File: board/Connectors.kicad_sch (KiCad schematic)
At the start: 14 parts, among them J10 Bus_Hydra_8bit, J11 Bus_Hydra_8bit, J12 Bus_Hydra_8bit, J13 Bus_Hydra_8bit, J14 Bus_Hydra_8bit, J16 SPI_Dev0, J18 SPI_Dev1, J19 SPI_Dev2, J20 SPI_Dev3, J21 SPI_Dev4, J22 SPI_Dev5, J23 SPI_Dev6, J24 SPI_Dev7, J9 Bus_Hydra_8bit

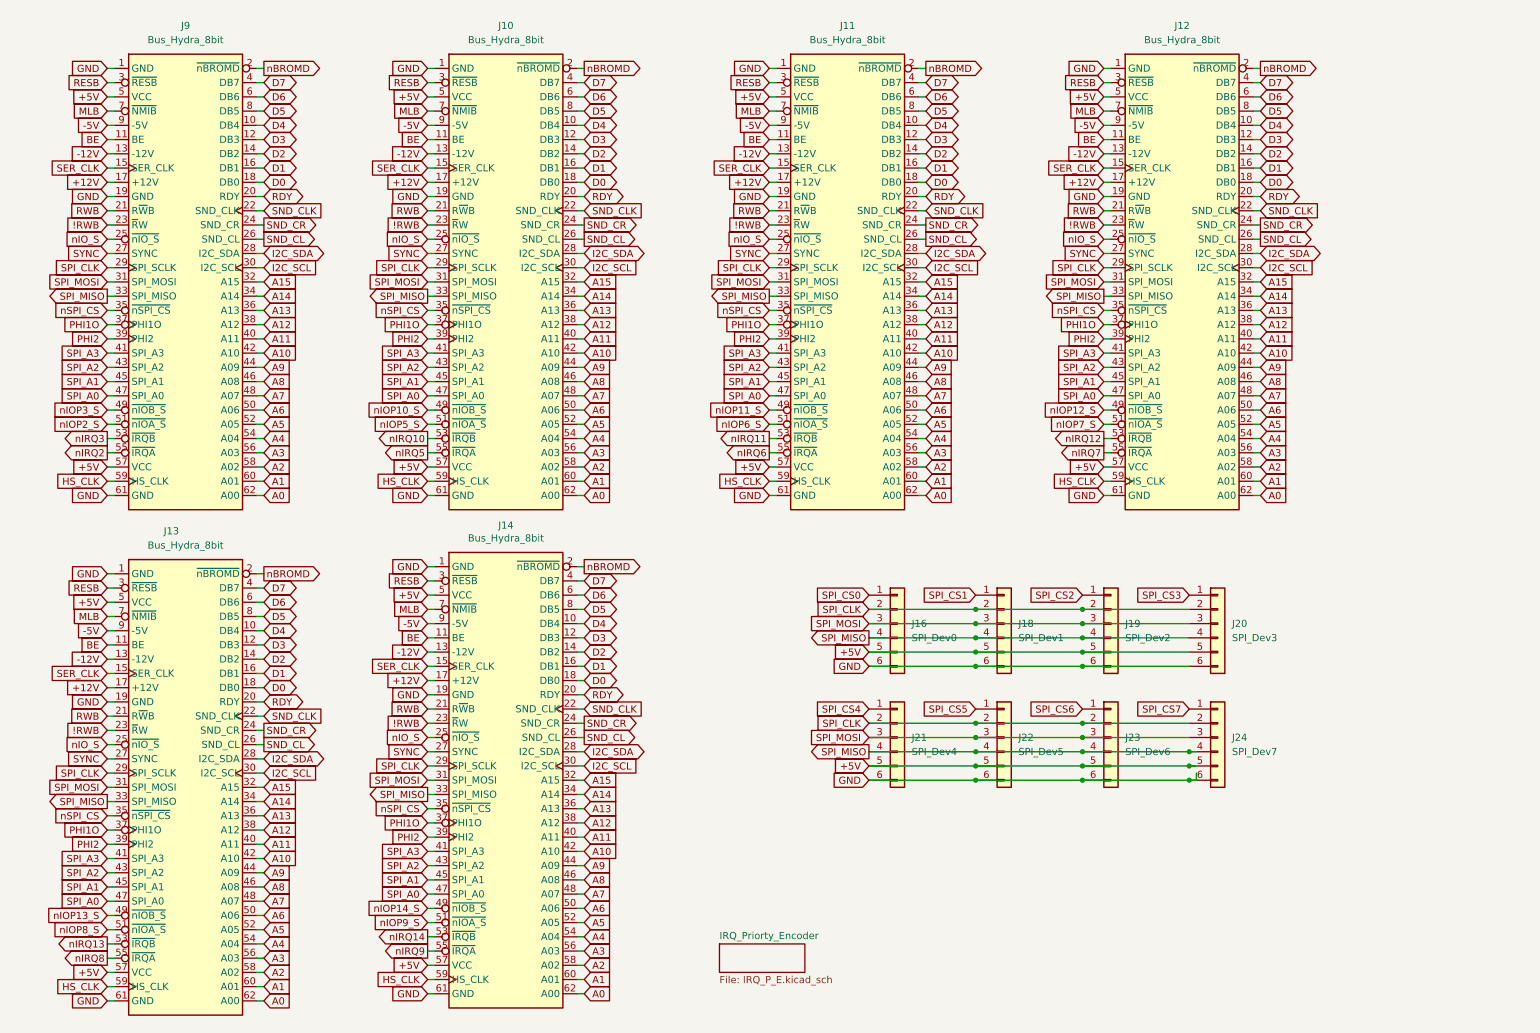
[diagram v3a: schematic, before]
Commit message: Schematic Bus updates, silkscreen updates, position tweaks, and other corrections.
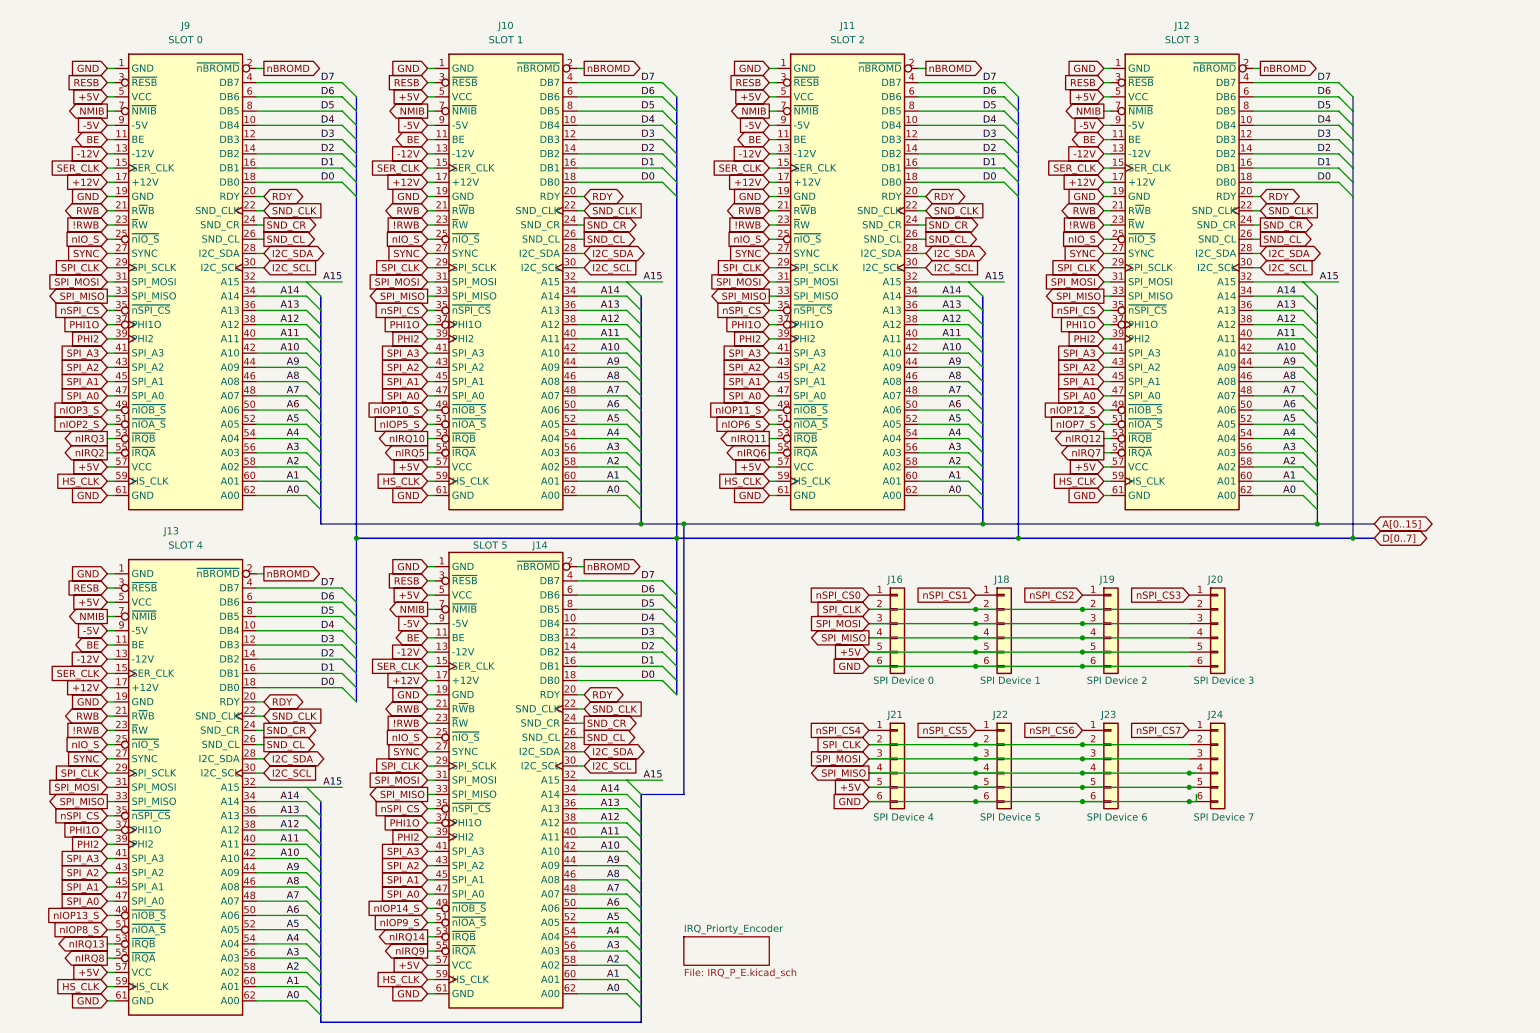
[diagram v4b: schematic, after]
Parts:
- J10: value Bus_Hydra_8bit -> SLOT 1
- J11: value Bus_Hydra_8bit -> SLOT 2
- J12: value Bus_Hydra_8bit -> SLOT 3
- J13: value Bus_Hydra_8bit -> SLOT 4
- J14: value Bus_Hydra_8bit -> SLOT 5
- J16: value SPI_Dev0 -> SPI Device 0
- J18: value SPI_Dev1 -> SPI Device 1
- J19: value SPI_Dev2 -> SPI Device 2
- J20: value SPI_Dev3 -> SPI Device 3
- J21: value SPI_Dev4 -> SPI Device 4
- J22: value SPI_Dev5 -> SPI Device 5
- J23: value SPI_Dev6 -> SPI Device 6
- J24: value SPI_Dev7 -> SPI Device 7
- J9: value Bus_Hydra_8bit -> SLOT 0
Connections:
- net MLB renamed NMIB
- net SPI_CS0 renamed nSPI_CS0
- net SPI_CS1 renamed nSPI_CS1
- net SPI_CS2 renamed nSPI_CS2
- net SPI_CS3 renamed nSPI_CS3
- net SPI_CS4 renamed nSPI_CS4
- net SPI_CS5 renamed nSPI_CS5
- net SPI_CS6 renamed nSPI_CS6
- net SPI_CS7 renamed nSPI_CS7
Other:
- company: (none) -> Data Tuning
- title: (none) -> Card-edge and SPI Device Connectors
- moved on the sheet: J21, J22, J23, J24

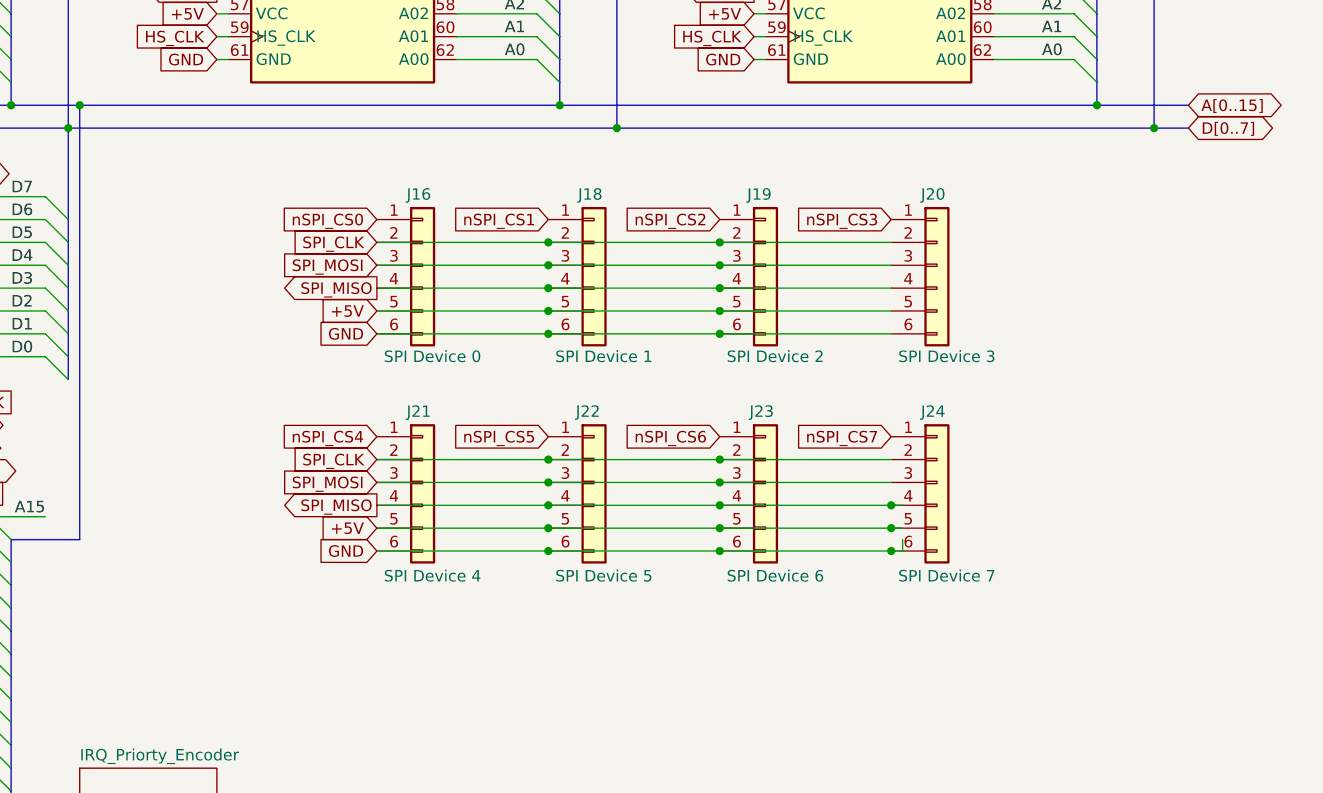
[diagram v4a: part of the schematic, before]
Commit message: Added VIA port A header and voltage protection diode package socket. Updated logic.
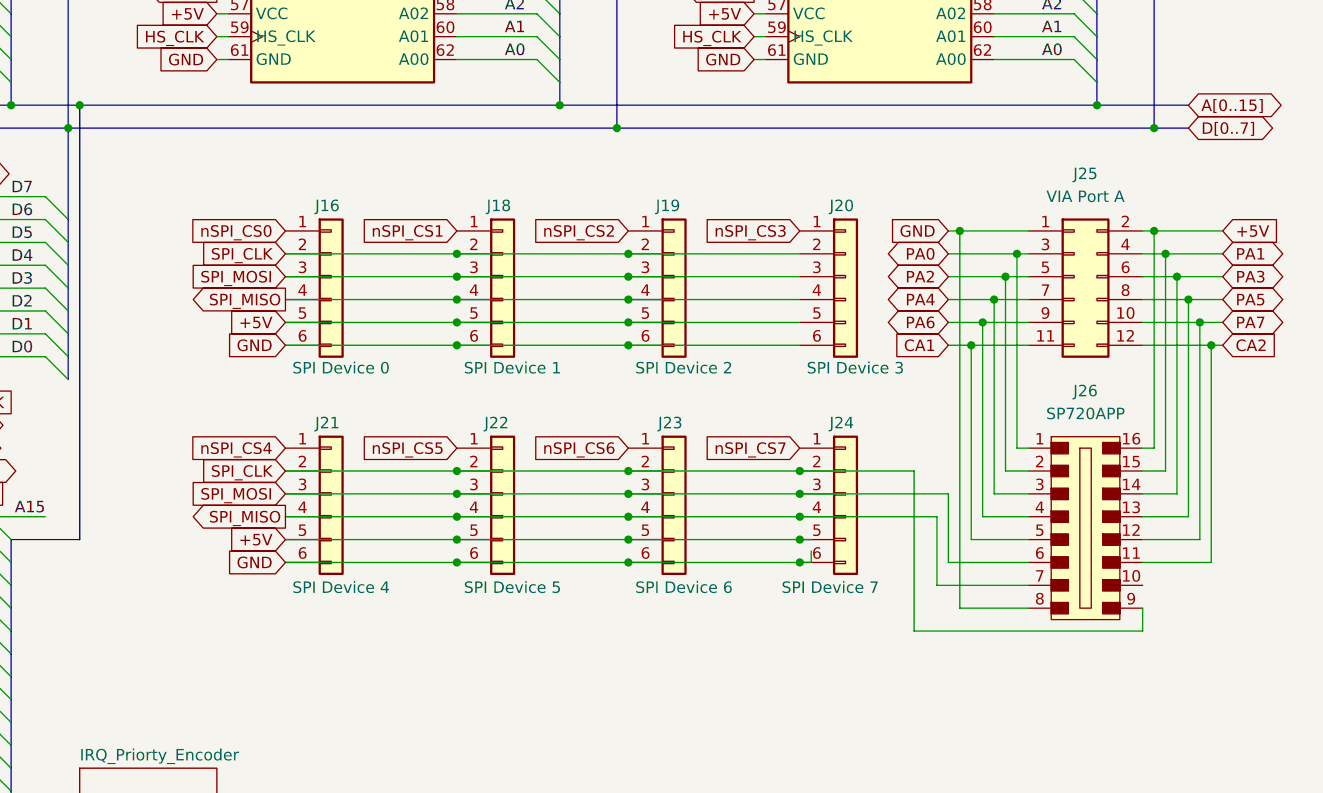
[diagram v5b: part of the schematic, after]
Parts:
- added J25: VIA Port A, Connector_PinHeader_2.54mm:PinHeader_2x06_P2.54mm_Vertical, symbol Connector_Generic:Conn_02x06_Odd_Even
- added J26: SP720APP, Package_DIP:DIP-16_W7.62mm_Socket_LongPads, symbol dk_Sockets-for-ICs-Transistors:A_16-LC-TT
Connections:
- net +5V: now also J25.2 (Pin_2), J26.16
- net GND: now also J25.1 (Pin_1), J26.8
- net SPI_CLK: now also J26.9
- net SPI_MISO: now also J26.7
- net SPI_MOSI: now also J26.6
- new net CA1: J25.11 (Pin_11), J26.5
- new net CA2: J25.12 (Pin_12), J26.11
- new net PA0: J25.3 (Pin_3), J26.1
- new net PA1: J25.4 (Pin_4), J26.15
- new net PA2: J25.5 (Pin_5), J26.2
- new net PA3: J25.6 (Pin_6), J26.14
- new net PA4: J25.7 (Pin_7), J26.3
- new net PA5: J25.8 (Pin_8), J26.13
- new net PA6: J25.9 (Pin_9), J26.4
- new net PA7: J25.10 (Pin_10), J26.12
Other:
- moved on the sheet: J16, J18, J19, J20, J21, J22, J23, J24

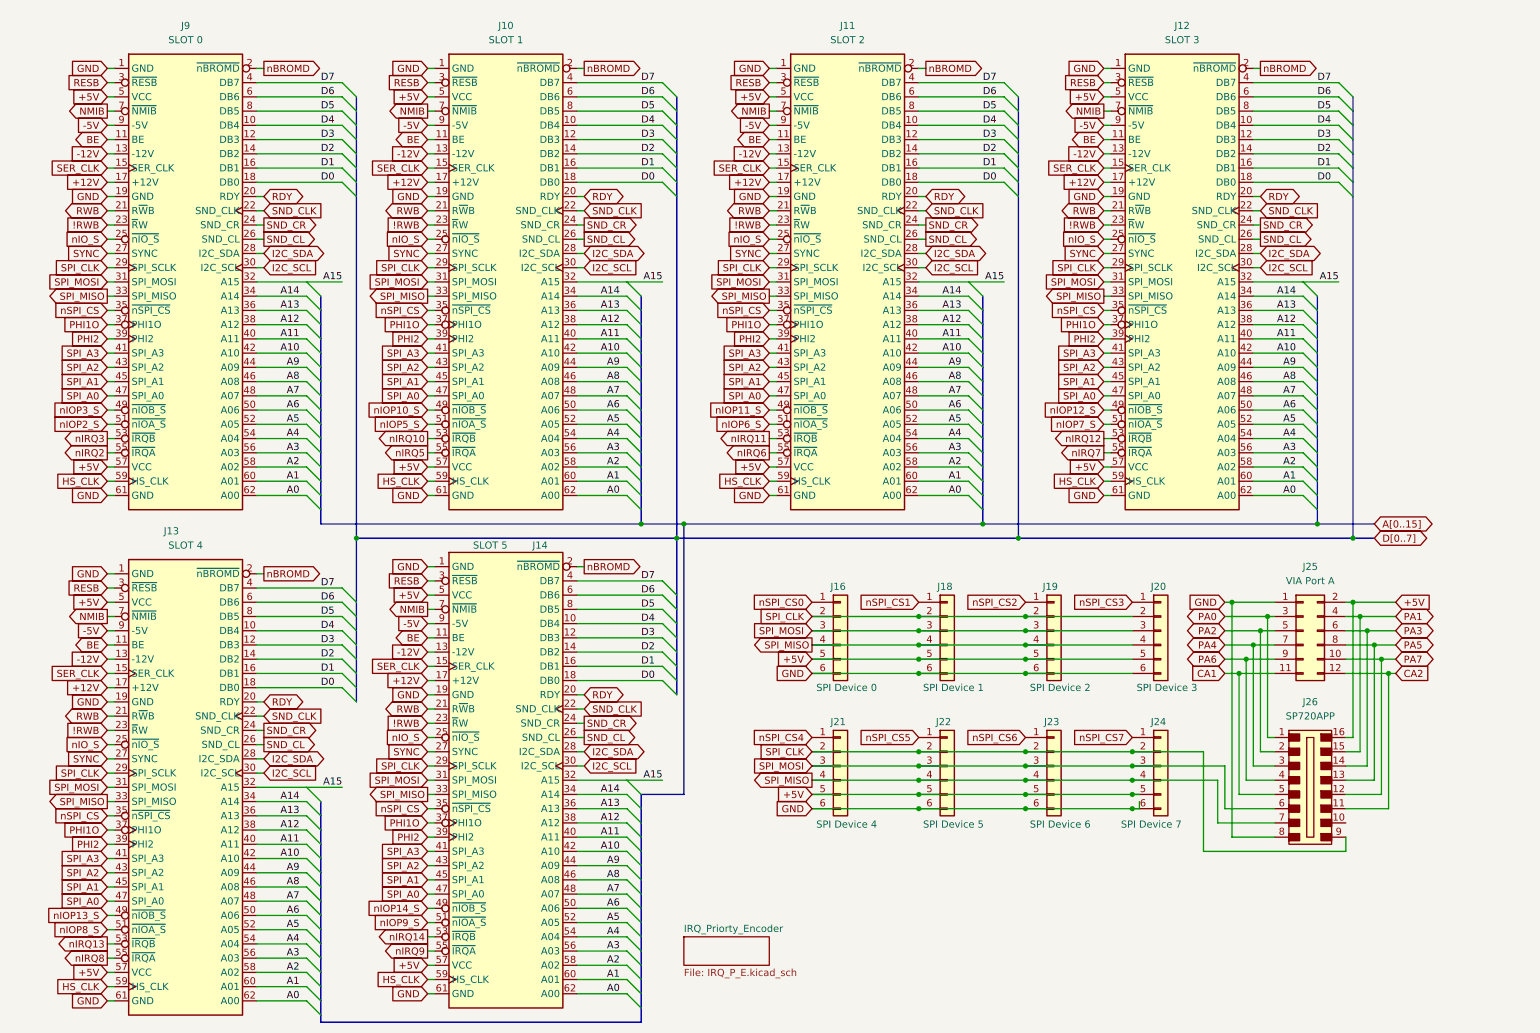
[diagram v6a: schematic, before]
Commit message: Fixing A9 routing on main schematic, and adding new footprint for the DSUB-9 serial connector.
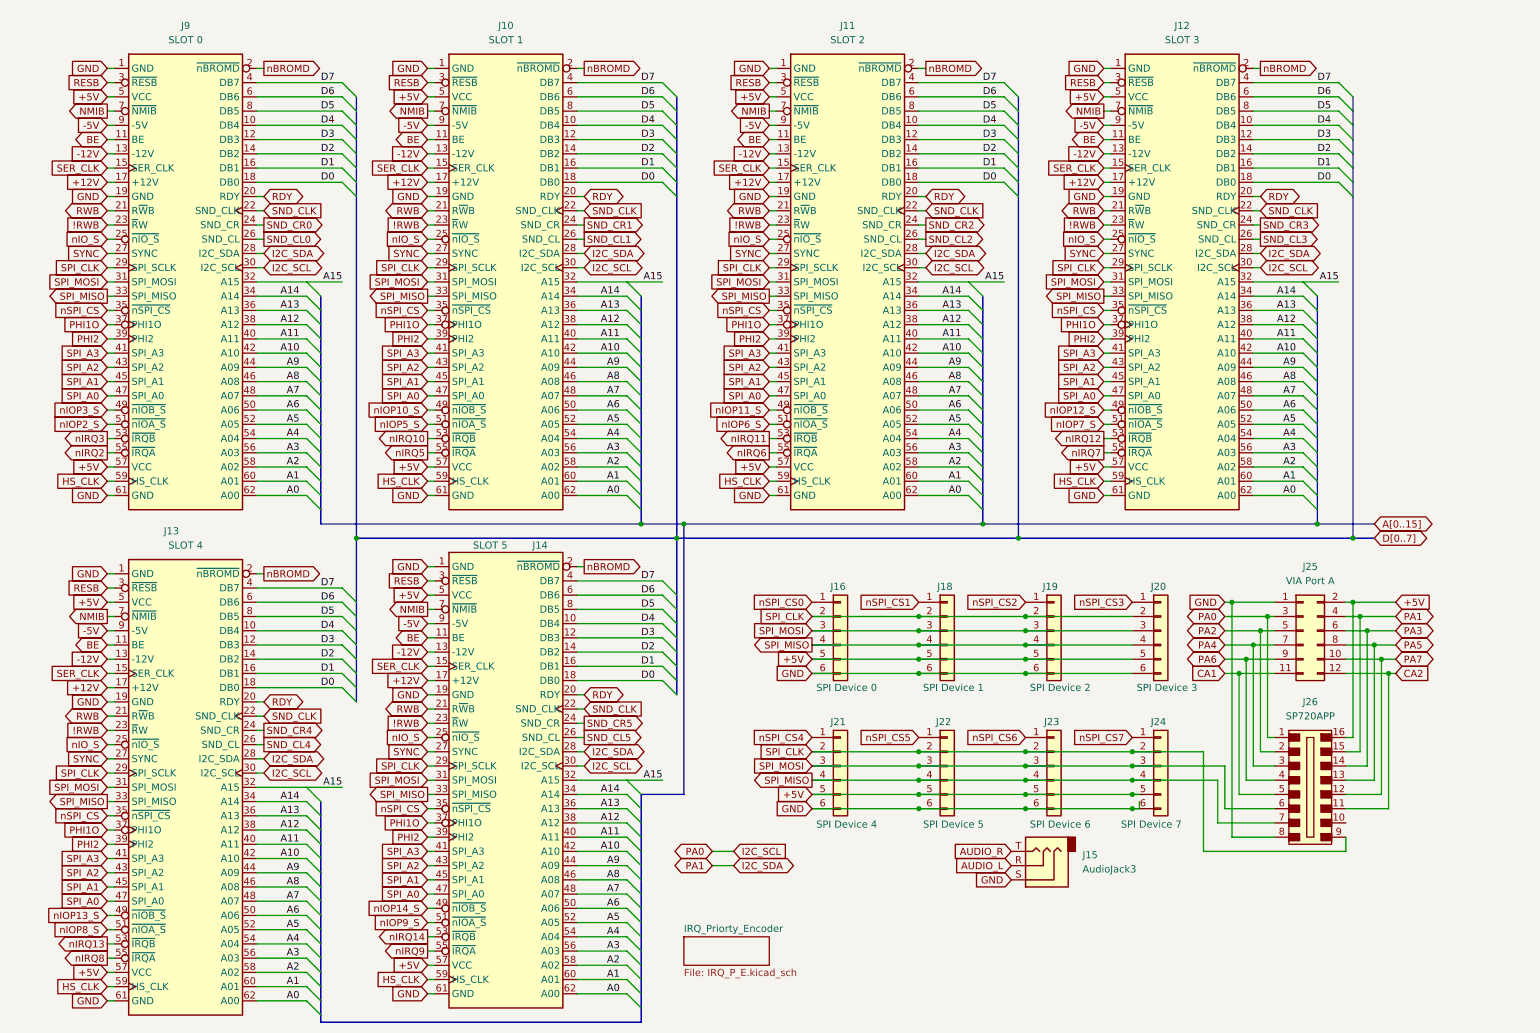
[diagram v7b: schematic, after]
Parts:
- added J15: AudioJack3, Connector_Audio:Jack_3.5mm_CUI_SJ1-3523N_Horizontal, symbol Connector_Audio:AudioJack3
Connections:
- net PA0 is gone; now on net I2C_SCL: J25.3 (Pin_3), J26.1
- net PA1 is gone; now on net I2C_SDA: J25.4 (Pin_4), J26.15
- net GND: now also J15.S
- removed net SND_CL: J10.26 (SND_CL), J11.26 (SND_CL), J12.26 (SND_CL), J13.26 (SND_CL), J14.26 (SND_CL), J9.26 (SND_CL)
- removed net SND_CR: J10.24 (SND_CR), J11.24 (SND_CR), J12.24 (SND_CR), J13.24 (SND_CR), J14.24 (SND_CR), J9.24 (SND_CR)
- new net AUDIO_L: J15.R
- new net AUDIO_R: J15.T
- new net SND_CL0: J9.26 (SND_CL)
- new net SND_CL1: J10.26 (SND_CL)
- new net SND_CL2: J11.26 (SND_CL)
- new net SND_CL3: J12.26 (SND_CL)
- new net SND_CL4: J13.26 (SND_CL)
- new net SND_CL5: J14.26 (SND_CL)
- new net SND_CR0: J9.24 (SND_CR)
- new net SND_CR1: J10.24 (SND_CR)
- new net SND_CR2: J11.24 (SND_CR)
- new net SND_CR3: J12.24 (SND_CR)
- new net SND_CR4: J13.24 (SND_CR)
- new net SND_CR5: J14.24 (SND_CR)
